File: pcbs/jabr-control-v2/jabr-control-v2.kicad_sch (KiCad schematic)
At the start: 4 parts

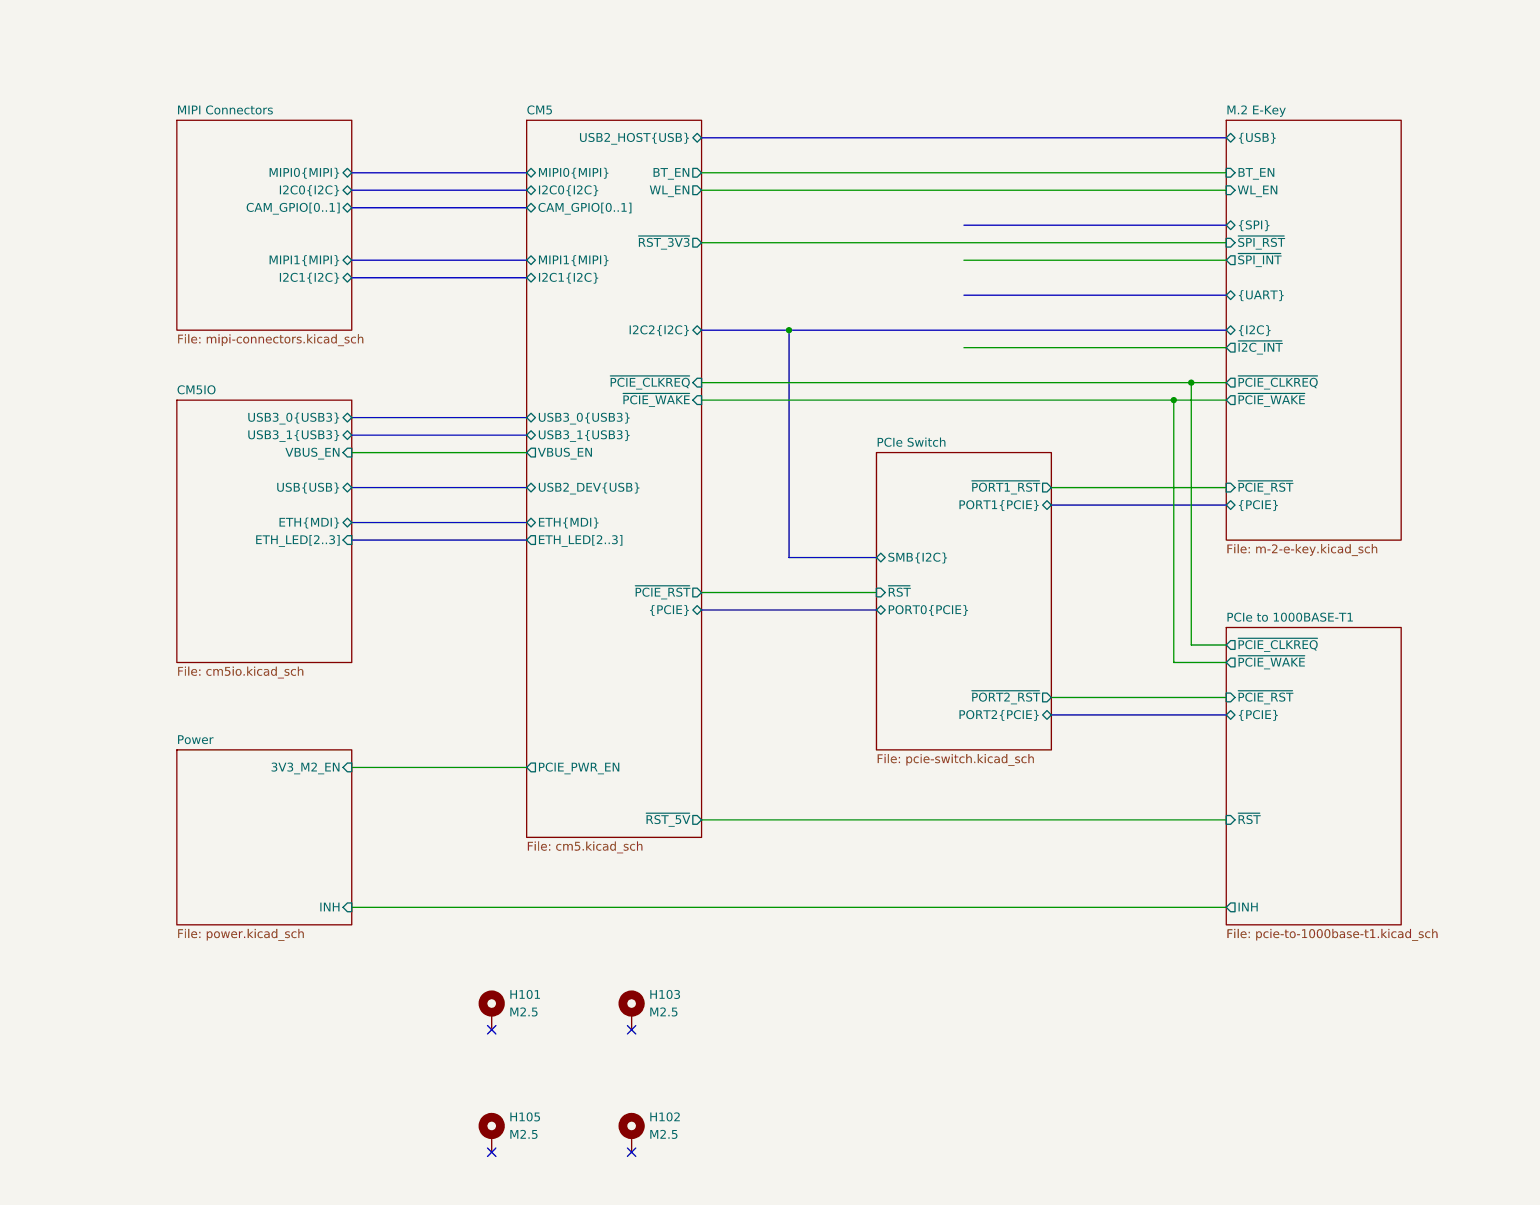
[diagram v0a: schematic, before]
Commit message: PCI11010C Schematic sheet mostly done
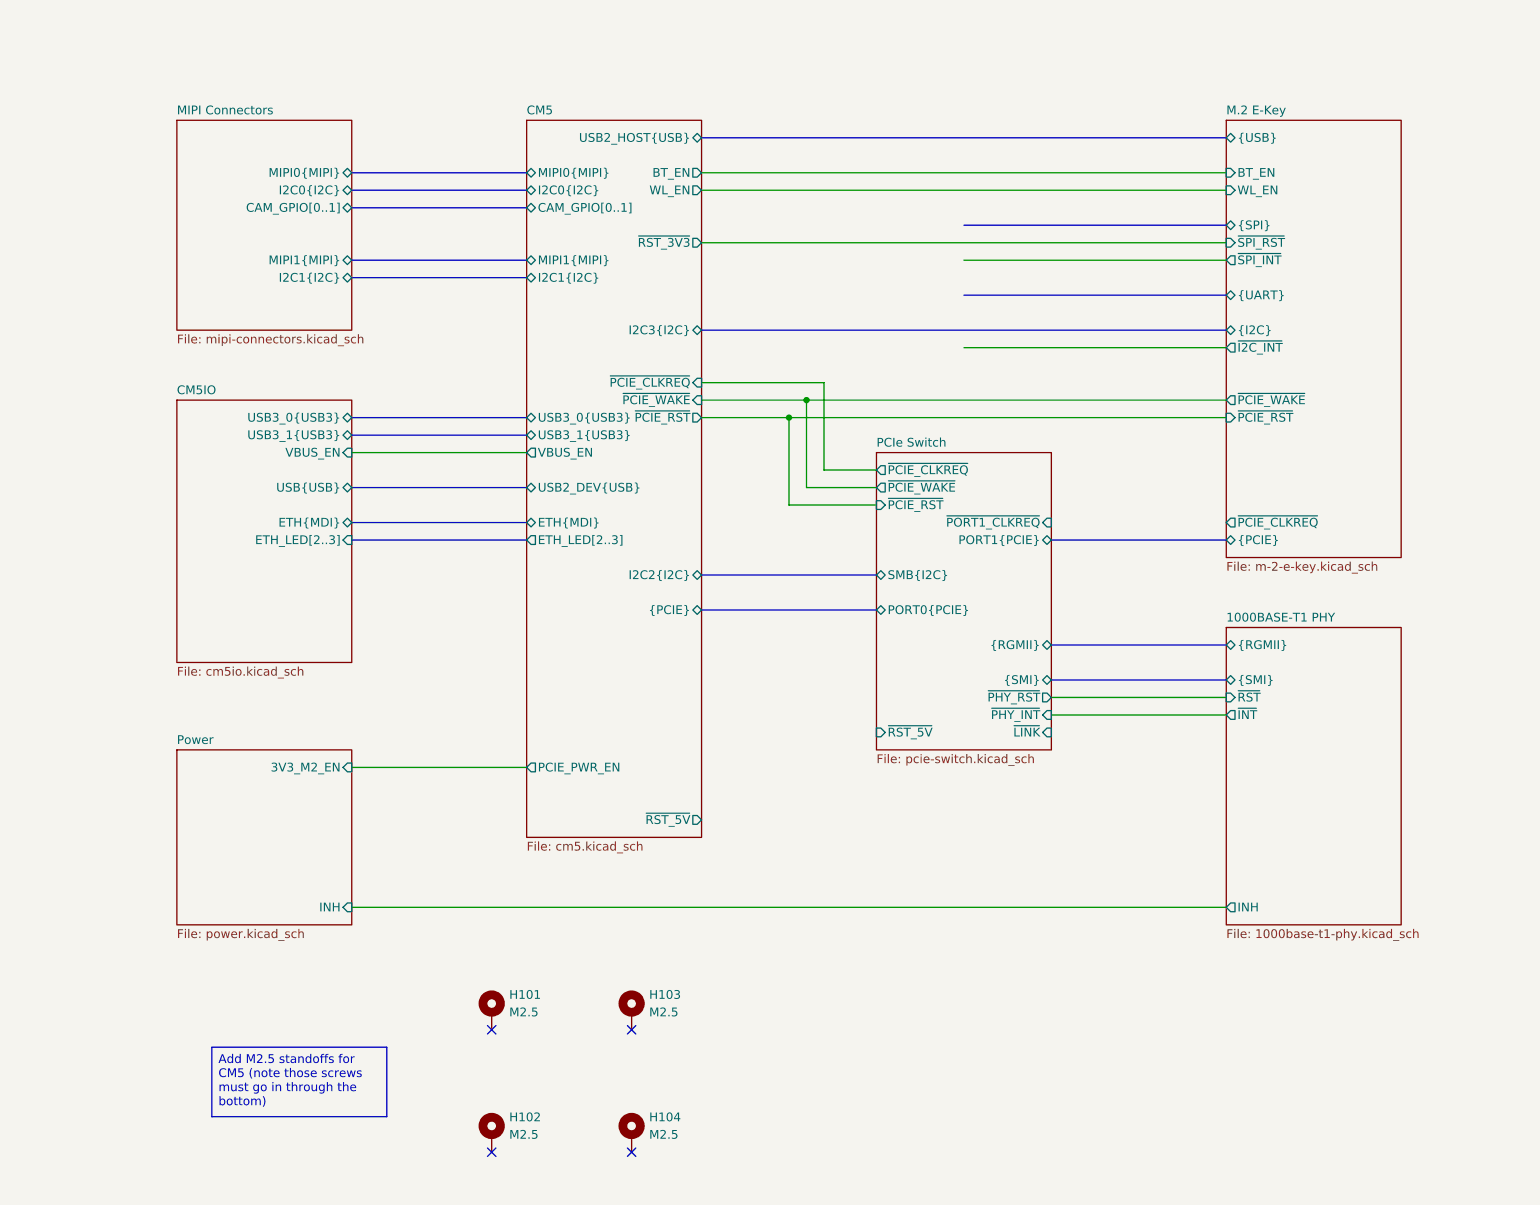
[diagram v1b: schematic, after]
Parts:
- renumbered H105 to H102, H102 to H104
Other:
- removed sheet PCIe to 1000BASE-T1
- added sheet 1000BASE-T1 PHY (1000base-t1-phy.kicad_sch)
- sheet CM5 ports: added I2C3{I2C}; removed none
- sheet PCIe Switch ports: added {RGMII}, {SMI}, ~{LINK}, ~{PCIE_CLKREQ}, ~{PCIE_RST}, ~{PCIE_WAKE}, ~{PHY_INT}, ~{PHY_RST}, ~{PORT1_CLKREQ}, ~{RST_5V}; removed PORT2{PCIE}, ~{PORT1_RST}, ~{PORT2_RST}, ~{RST}

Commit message: Moved M.2 buffers to new sheet
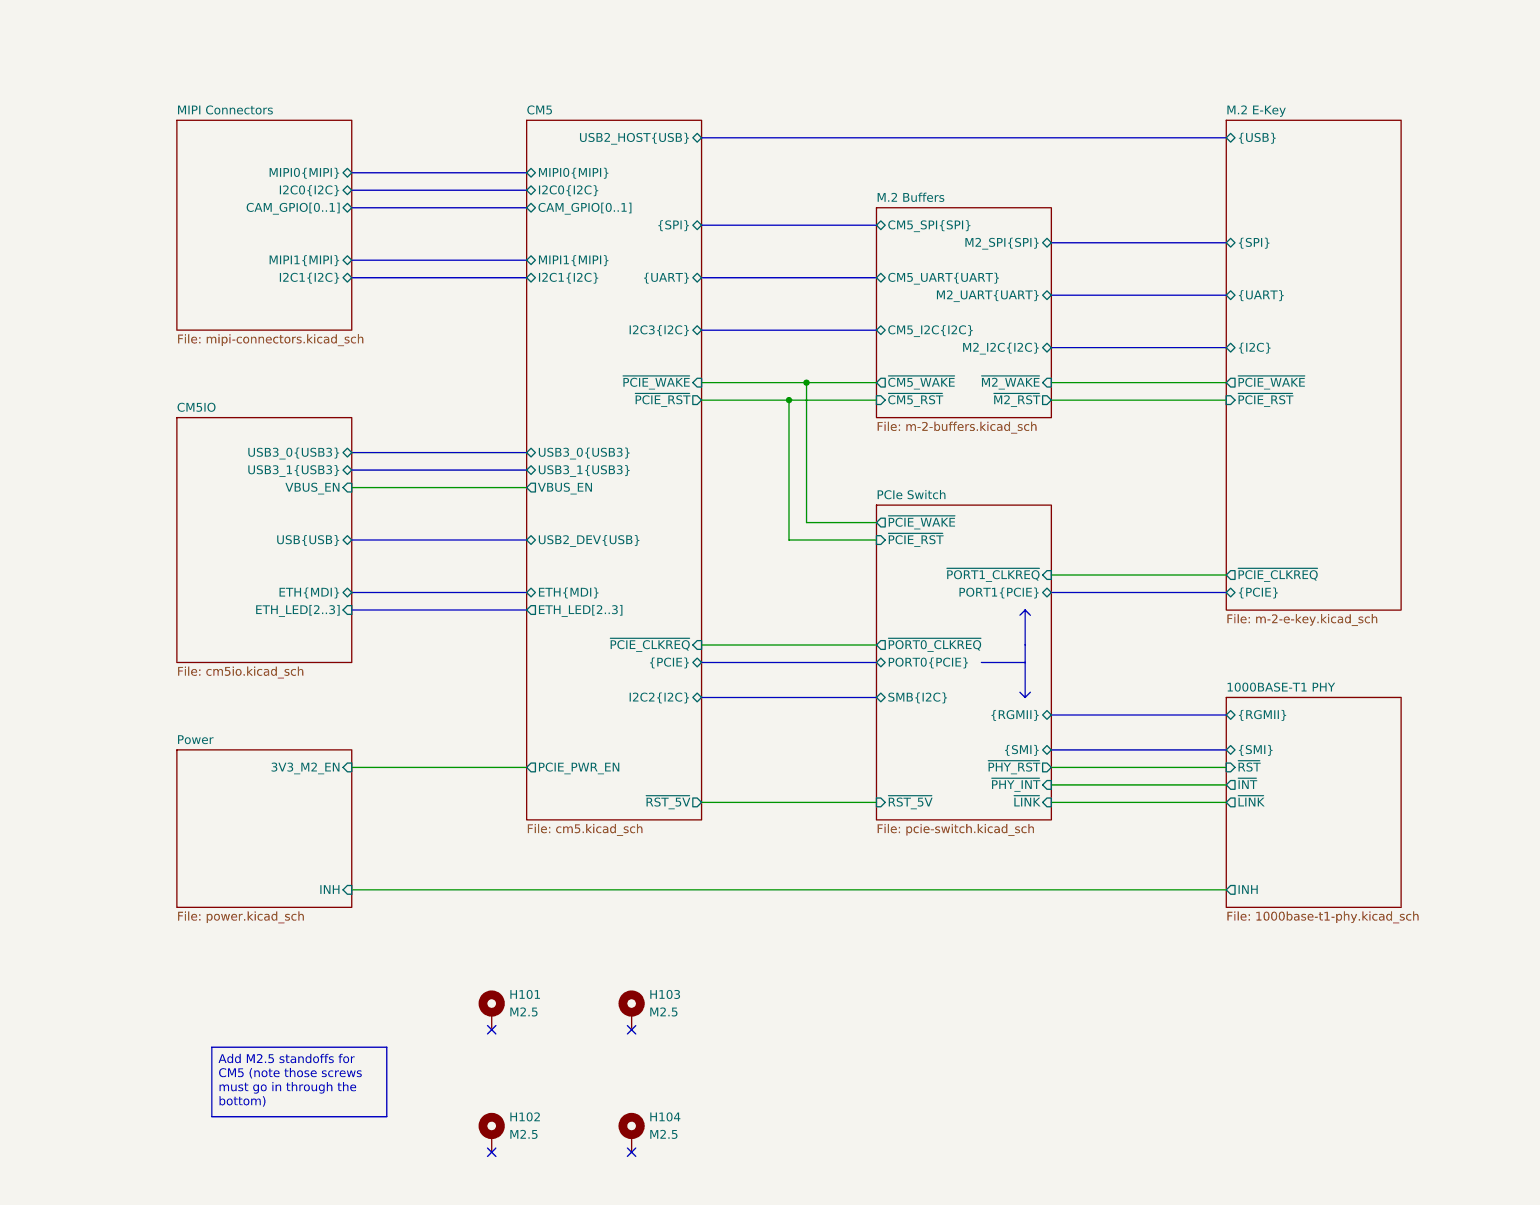
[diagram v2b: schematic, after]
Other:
- added sheet M.2 Buffers (m-2-buffers.kicad_sch)
- sheet 1000BASE-T1 PHY ports: added ~{LINK}; removed none
- sheet CM5 ports: added {SPI}, {UART}; removed BT_EN, WL_EN, ~{RST_3V3}
- sheet M.2 E-Key ports: added none; removed BT_EN, WL_EN, ~{I2C_INT}, ~{SPI_INT}, ~{SPI_RST}
- sheet PCIe Switch ports: added ~{PORT0_CLKREQ}; removed ~{PCIE_CLKREQ}

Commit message: Power circuitry done
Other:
- sheet PCIe Switch ports: added ~{PCIE_PG}; removed none
- sheet Power ports: added PCIE_PG, PCIE_PWR_EN; removed 3V3_M2_EN
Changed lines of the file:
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@@
+	(wire
+		(pts
+			(xy 152.4 144.78) (xy 88.9 144.78)
+		)
+		(stroke
+			(width 0)
+			(type default)
+		)
+	)
 	(wire
 		(pts
@@
 	(wire
 		(pts
-			(xy 139.7 137.16) (xy 165.1 137.16)
+			(xy 139.7 132.08) (xy 165.1 132.08)
 		)
 		(stroke
@@
 	(wire
 		(pts
+			(xy 165.1 134.62) (xy 152.4 134.62)
+		)
+		(stroke
+			(width 0)
+			(type default)
+		)
+	)
+	(wire
+		(pts
 			(xy 88.9 91.44) (xy 114.3 91.44)
 		)
@@
 		(pts
 			(xy 190.5 71.12) (xy 215.9 71.12)
+		)
+		(stroke
+			(width 0)
+			(type default)
+		)
+	)
+	(wire
+		(pts
+			(xy 152.4 134.62) (xy 152.4 144.78)
 		)
 		(stroke
@@
 			)
 		)
-		(pin "3V3_M2_EN" input
-			(at 88.9 132.08 0)
-			(effects
-				(font
-					(size 1.27 1.27)
-				)
-				(justify right)
-			)
-		)
 		(pin "INH" input
 			(at 88.9 149.86 0)
+			(effects
+				(font
+					(size 1.27 1.27)
+				)
+				(justify right)
+			)
+		)
+		(pin "PCIE_PG" output
+			(at 88.9 144.78 0)
+			(effects
+				(font
+					(size 1.27 1.27)
+				)
+				(justify right)
+			)
+		)
+		(pin "PCIE_PWR_EN" input
+			(at 88.9 132.08 0)
 			(effects
 				(font
@@
 		)
 		(pin "~{RST_5V}" input
-			(at 165.1 137.16 180)
+			(at 165.1 132.08 180)
 			(effects
 				(font
@@
 		(pin "~{PORT0_CLKREQ}" output
 			(at 165.1 114.3 180)
+			(effects
+				(font
+					(size 1.27 1.27)
+				)
+				(justify left)
+			)
+		)
+		(pin "~{PCIE_PG}" input
+			(at 165.1 134.62 180)
 			(effects
 				(font
@@
 	(sheet
 		(at 114.3 38.1)
-		(size 25.4 101.6)
+		(size 25.4 96.52)
 		(exclude_from_sim no)
 		(in_bom yes)
@@
 		)
 		(property "Sheetfile" "cm5.kicad_sch"
-			(at 114.3 140.2846 0)
+			(at 114.3 135.2046 0)
 			(show_name no)
 			(do_not_autoplace no)
@@
 		)
 		(pin "~{RST_5V}" output
-			(at 139.7 137.16 0)
-			(effects
-				(font
+			(at 139.7 132.08 0)
+			(effects
+				(font

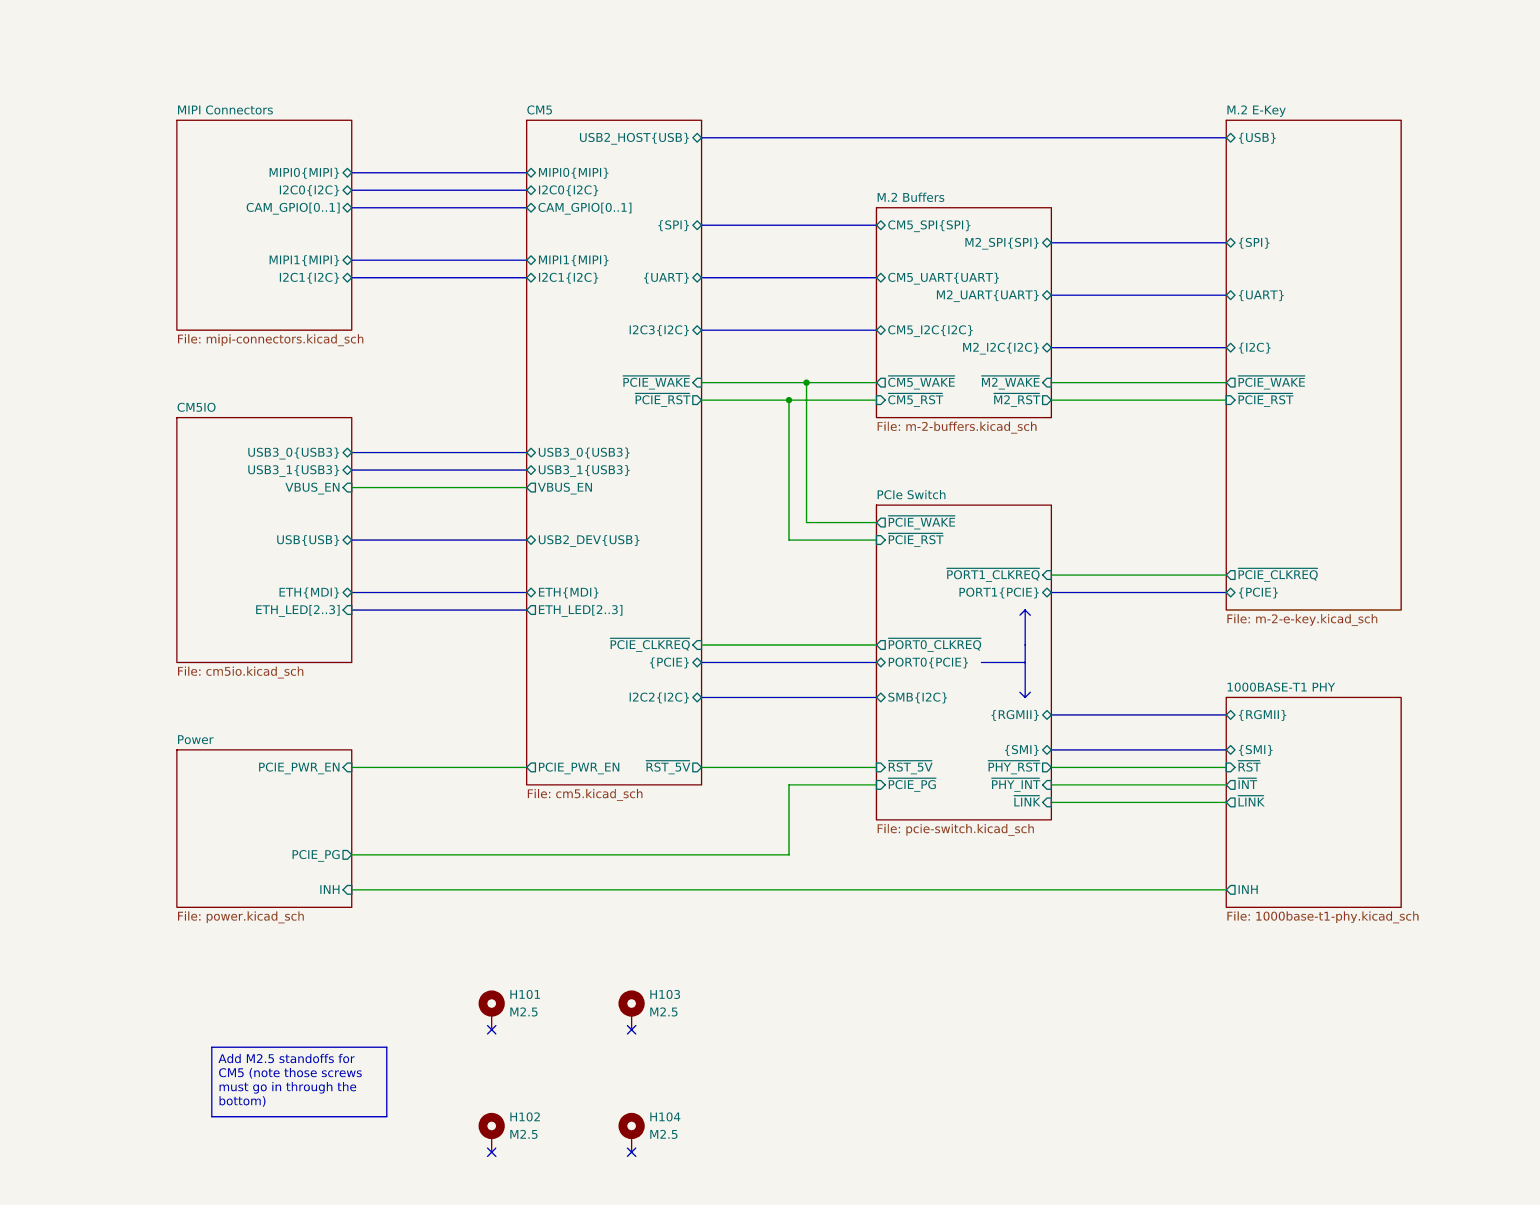
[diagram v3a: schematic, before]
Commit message: PCI11010 IO done
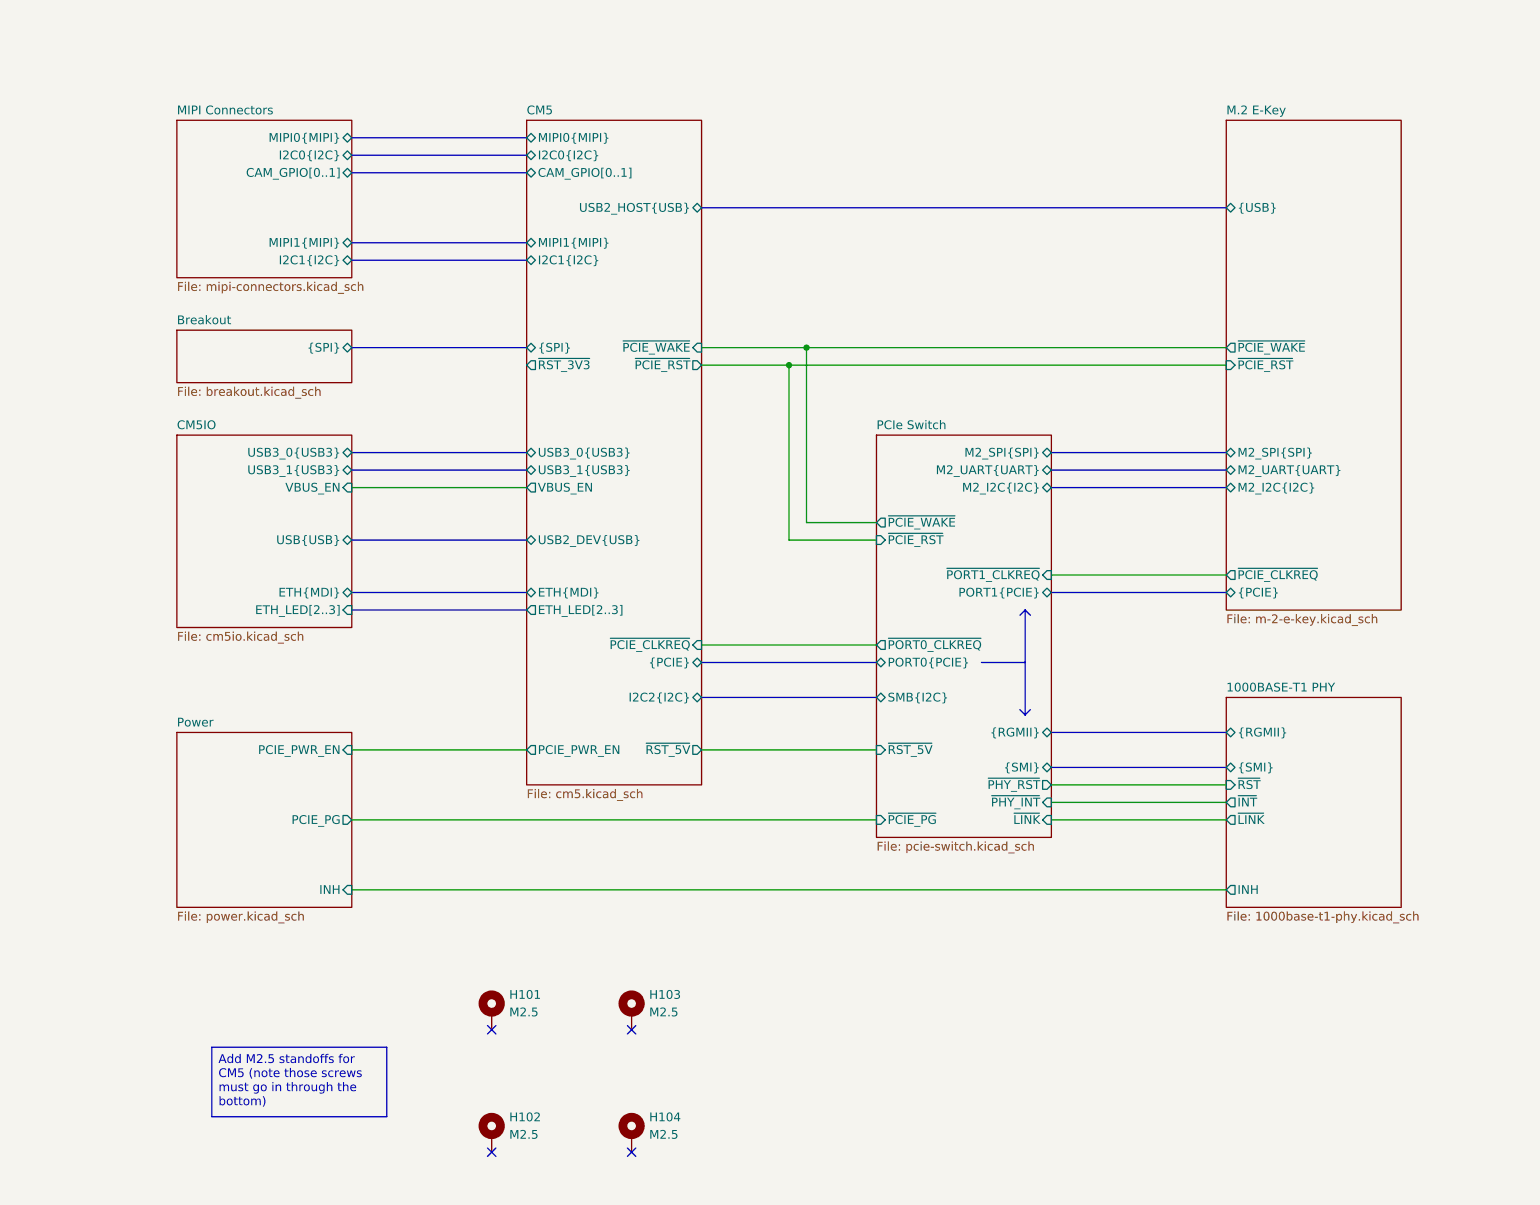
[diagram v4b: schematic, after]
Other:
- removed sheet M.2 Buffers
- added sheet Breakout (breakout.kicad_sch)
- sheet CM5 ports: added ~{RST_3V3}; removed I2C3{I2C}, {UART}
- sheet M.2 E-Key ports: added M2_I2C{I2C}, M2_SPI{SPI}, M2_UART{UART}; removed {I2C}, {SPI}, {UART}
- sheet PCIe Switch ports: added M2_I2C{I2C}, M2_SPI{SPI}, M2_UART{UART}; removed none
